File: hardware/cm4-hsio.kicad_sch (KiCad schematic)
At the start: 1 part, among them J1 DF40C-100DP-0.4V_51_

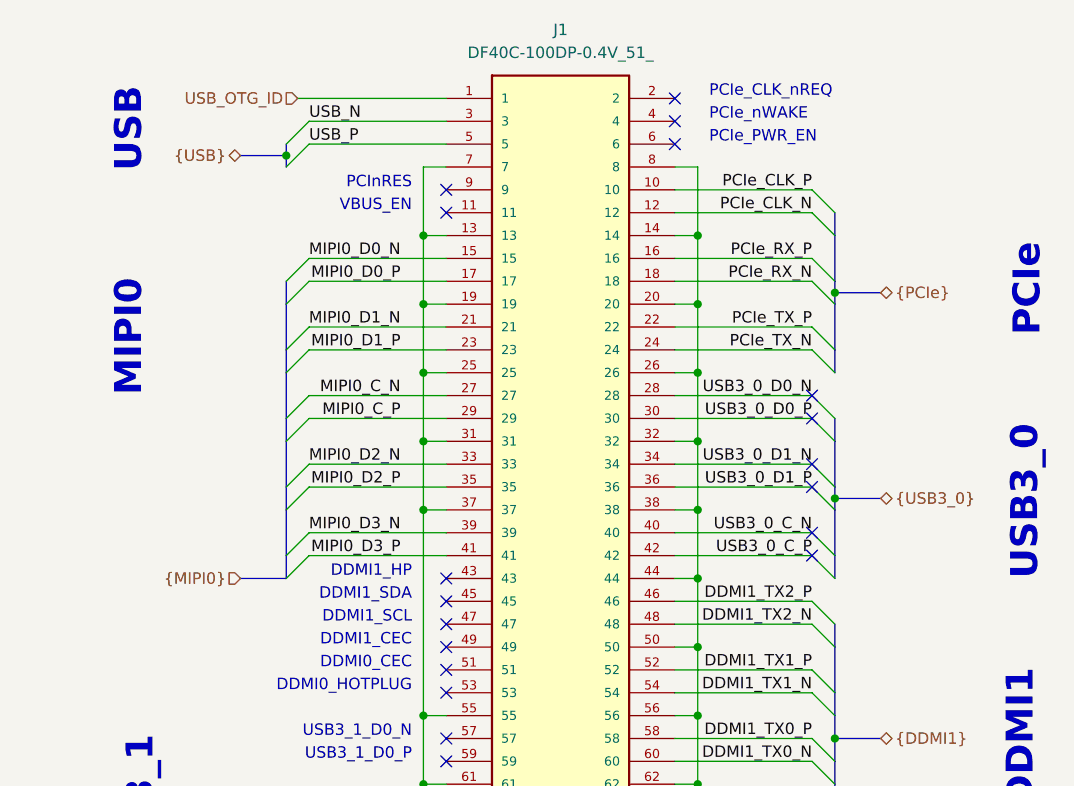
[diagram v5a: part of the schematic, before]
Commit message: Clearing all ERC, rounting diff
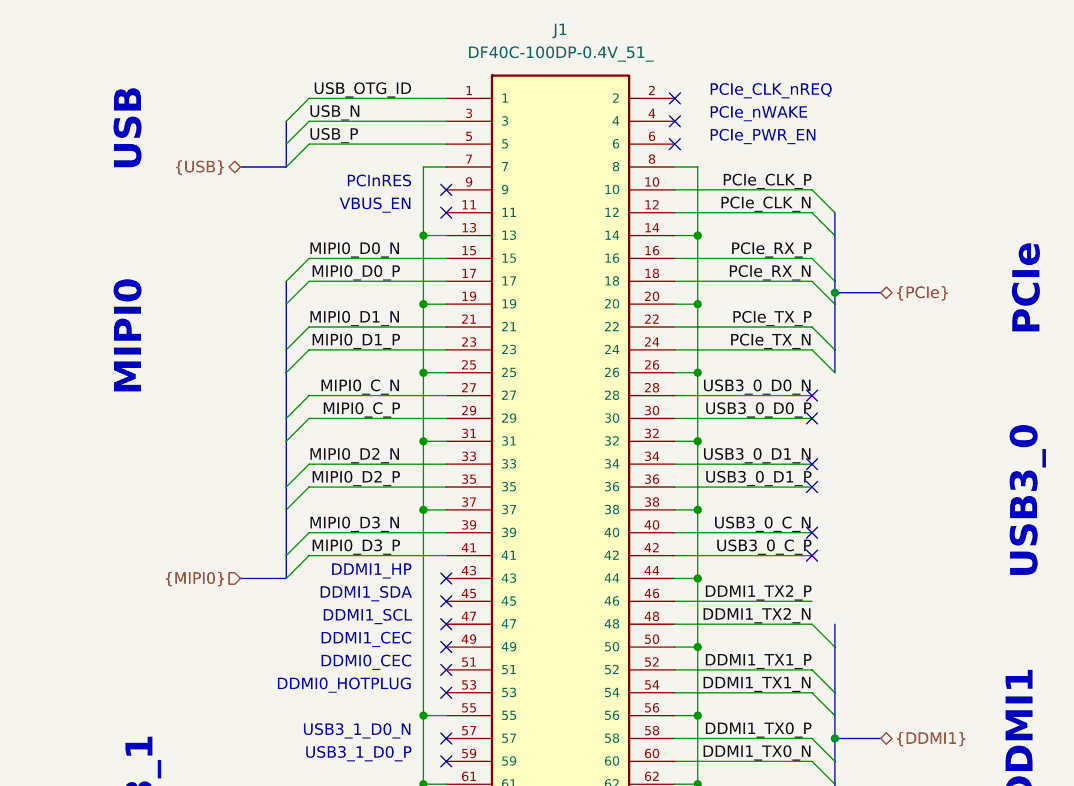
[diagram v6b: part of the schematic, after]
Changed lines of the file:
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@@
 		(comment 1 "${project_license}")
 	)
-	(bus_alias "CAM0"
-		(members "CAM0_D0_P" "CAM0_D0_N" "CAM0_D1_P" "CAM0_D1_N" "CAM0_D2_P" "CAM0_D2_N"
-			"CAM0_C_P" "CAM0_C_N"
+	(bus_alias "MIPI0"
+		(members "MIPI0_D0_P" "MIPI0_D0_N" "MIPI0_D1_P" "MIPI0_D1_N" "MIPI0_D2_P"
+			"MIPI0_D2_N" "MIPI0_C_P" "MIPI0_C_N" "MIPI0_D3_P" "MIPI0_D3_N"
+		)
+	)
+	(bus_alias "MIPI1"
+		(members "MIPI1_D0_P" "MIPI1_D0_N" "MIPI1_D1_P" "MIPI1_D1_N" "MIPI1_D2_P"
+			"MIPI1_D2_N" "MIPI1_D3_P" "MIPI1_D3_N" "MIPI1_C_P" "MIPI1_C_N"
 		)
 	)
@@
 	)
 	(bus_alias "USB"
-		(members "USB_P" "USB_N")
+		(members "USB_N" "USB_P" "USB_OTG_ID")
 	)
 	(text "USB3_0"
@@
 	)
 	(junction
-		(at 182.88 72.39)
-		(diameter 0)
-		(color 0 0 0 0)
-	)
-	(junction
 		(at 167.64 66.04)
-		(diameter 0)
-		(color 0 0 0 0)
-	)
-	(junction
-		(at 121.92 34.29)
 		(diameter 0)
 		(color 0 0 0 0)
@@
 	)
 	(bus_entry
-		(at 180.34 68.58)
-		(size 2.54 2.54)
-		(stroke
-			(width 0)
-			(type default)
-		)
-	)
-	(bus_entry
 		(at 180.34 139.7)
 		(size 2.54 2.54)
@@
 	)
 	(bus_entry
-		(at 180.34 60.96)
-		(size 2.54 2.54)
-		(stroke
-			(width 0)
-			(type default)
-		)
-	)
-	(bus_entry
-		(at 180.34 83.82)
-		(size 2.54 2.54)
-		(stroke
-			(width 0)
-			(type default)
-		)
-	)
-	(bus_entry
 		(at 121.92 48.26)
 		(size 2.54 -2.54)
@@
 	)
 	(bus_entry
-		(at 180.34 78.74)
-		(size 2.54 2.54)
-		(stroke
-			(width 0)
-			(type default)
-		)
-	)
-	(bus_entry
 		(at 121.92 63.5)
 		(size 2.54 -2.54)
@@
 	)
 	(bus_entry
-		(at 180.34 76.2)
-		(size 2.54 2.54)
-		(stroke
-			(width 0)
-			(type default)
-		)
-	)
-	(bus_entry
 		(at 180.34 109.22)
 		(size 2.54 2.54)
@@
 	)
 	(bus_entry
+		(at 121.92 30.48)
+		(size 2.54 -2.54)
+		(stroke
+			(width 0)
+			(type default)
+		)
+	)
+	(bus_entry
 		(at 180.34 45.72)
 		(size 2.54 2.54)
@@
 	)
 	(bus_entry
-		(at 180.34 63.5)
-		(size 2.54 2.54)
-		(stroke
-			(width 0)
-			(type default)
-		)
-	)
-	(bus_entry
 		(at 121.92 66.04)
 		(size 2.54 -2.54)
@@
 	)
 	(bus_entry
-		(at 180.34 71.12)
-		(size 2.54 2.54)
-		(stroke
-			(width 0)
-			(type default)
-		)
-	)
-	(bus_entry
 		(at 180.34 129.54)
 		(size 2.54 2.54)
@@
 		)
 	)
+	(bus
+		(pts
+			(xy 121.92 30.48) (xy 121.92 33.02)
+		)
+		(stroke
+			(width 0)
+			(type default)
+		)
+	)
 	(wire
 		(pts
@@
 	(bus
 		(pts
-			(xy 182.88 71.12) (xy 182.88 72.39)
-		)
-		(stroke
-			(width 0)
-			(type default)
-		)
-	)
-	(bus
-		(pts
 			(xy 121.92 58.42) (xy 121.92 63.5)
 		)
@@
 		)
 	)
-	(bus
-		(pts
-			(xy 182.88 66.04) (xy 182.88 71.12)
-		)
-		(stroke
-			(width 0)
-			(type default)
-		)
-	)
 	(wire
 		(pts
@@
 	(bus
 		(pts
-			(xy 116.84 34.29) (xy 121.92 34.29)
+			(xy 116.84 35.56) (xy 121.92 35.56)
 		)
 		(stroke
@@
 		)
 	)
-	(bus
-		(pts
-			(xy 121.92 34.29) (xy 121.92 35.56)
-		)
-		(stroke
-			(width 0)
-			(type default)
-		)
-	)
 	(wire
 		(pts
@@
 		)
 	)
-	(bus
-		(pts
-			(xy 182.88 72.39) (xy 187.96 72.39)
-		)
-		(stroke
-			(width 0)
-			(type default)
-		)
-	)
 	(wire
 		(pts
@@
 	(wire
 		(pts
-			(xy 123.19 27.94) (xy 139.7 27.94)
+			(xy 124.46 27.94) (xy 139.7 27.94)
 		)
 		(stroke
@@
 	(bus
 		(pts
-			(xy 182.88 72.39) (xy 182.88 73.66)
-		)
-		(stroke
-			(width 0)
-			(type default)
-		)
-	)
-	(bus
-		(pts
 			(xy 182.88 134.62) (xy 187.96 134.62)
 		)
@@
 		)
 	)
-	(bus
-		(pts
-			(xy 182.88 63.5) (xy 182.88 66.04)
-		)
-		(stroke
-			(width 0)
-			(type default)
-		)
-	)
 	(wire
 		(pts
@@
 	(bus
 		(pts
-			(xy 121.92 33.02) (xy 121.92 34.29)
+			(xy 121.92 33.02) (xy 121.92 35.56)
 		)
 		(stroke
@@
 		)
 	)
-	(bus
-		(pts
-			(xy 182.88 73.66) (xy 182.88 78.74)
-		)
-		(stroke
-			(width 0)
-			(type default)
-		)
-	)
 	(wire
 		(pts
@@
 		(pts
 			(xy 165.1 104.14) (xy 167.64 104.14)
-		)
-		(stroke
-			(width 0)
-			(type default)
-		)
-	)
-	(bus
-		(pts
-			(xy 182.88 78.74) (xy 182.88 81.28)
 		)
 		(stroke
@@
 	(label "DDMI0_CLK_N"
 		(at 180.34 139.7 180)
+		(effects
+			(font
+				(size 1.27 1.27)
+			)
+			(justify right bottom)
+		)
+	)
+	(label "USB_OTG_ID"
+		(at 135.89 27.94 180)
 		(effects
 			(font
@@
 		)
 	)
-	(hierarchical_label "USB_OTG_ID"
-		(shape input)
-		(at 123.19 27.94 180)
-		(effects
-			(font
-				(size 1.27 1.27)
-			)
-			(justify right)
-		)
-	)
 	(hierarchical_label "{PCIe}"
 		(shape bidirectional)
@@
 		)
 	)
-	(hierarchical_label "{USB3_0}"
-		(shape bidirectional)
-		(at 187.96 72.39 0)
-		(effects
-			(font
-				(size 1.27 1.27)
-			)
-			(justify left)
-		)
-	)
 	(hierarchical_label "{MIPI1}"
 		(shape bidirectional)
@@
 	(hierarchical_label "{USB}"
 		(shape bidirectional)
-		(at 116.84 34.29 180)
-		(effects
-			(font
+		(at 116.84 35.56 180)
+		(effects
+			(font

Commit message: Cleanup
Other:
- moved on the sheet: J1

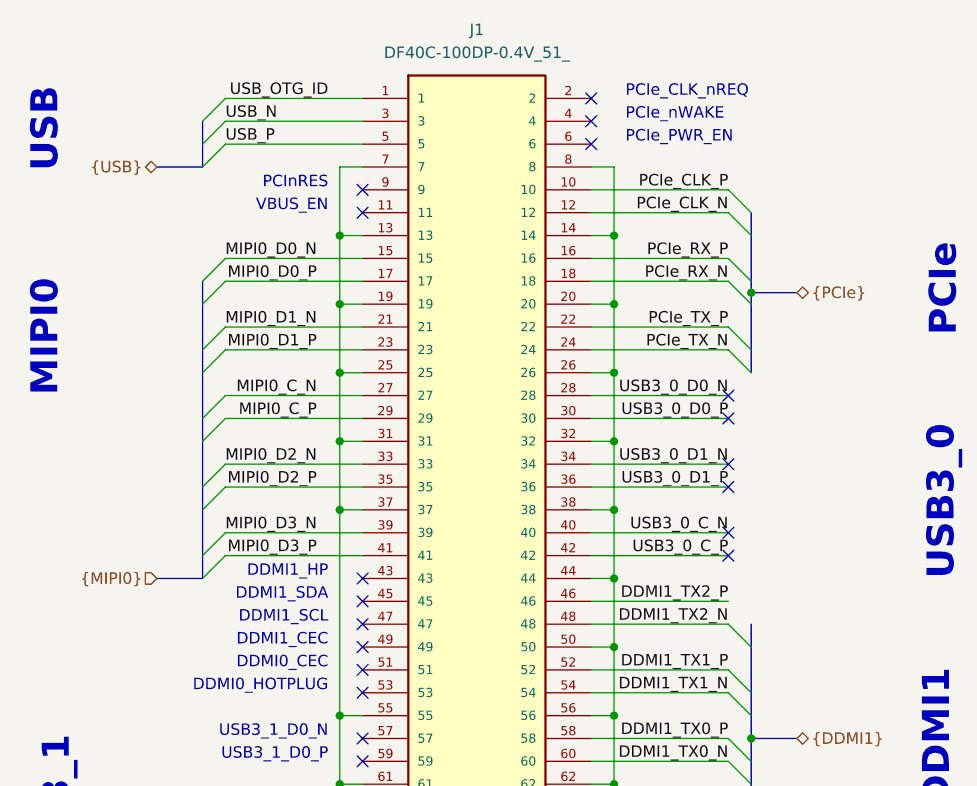
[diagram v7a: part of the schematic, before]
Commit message: GPIO are now routed differential
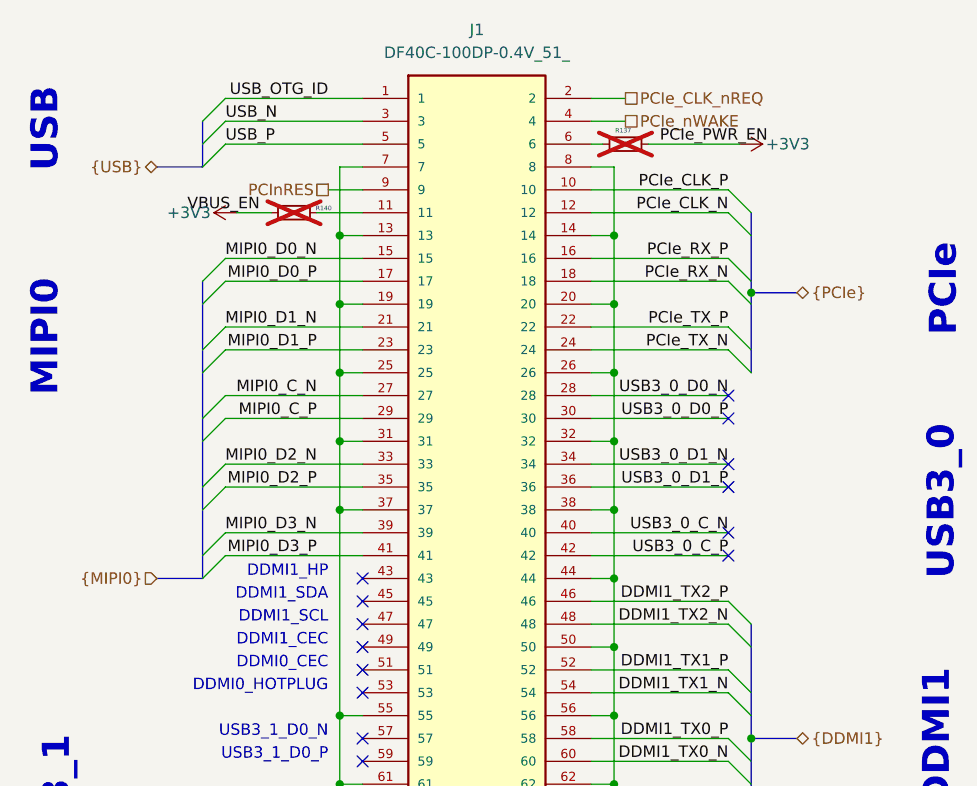
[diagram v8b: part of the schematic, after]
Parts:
- added R137, R140: 10k, Resistor_SMD:R_0402_1005Metric, symbol Device:R_Small
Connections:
- net at J1.11: now also R140.2
- net PCIe_CLK_nREQ: now reaches J1.2
- net PCIe_nWAKE: now reaches J1.4
- net at J1.6: now also R137.1
- net PCInRES: now reaches J1.9
- new net +3V3: R137.2, R140.1
- no-connect marks 25 -> 20
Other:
- note removed: "PCIe_CLK_nREQ"
- note removed: "PCIe_PWR_EN"
- note removed: "PCIe_nWAKE"
- note removed: "PCInRES"
- note removed: "VBUS_EN"
